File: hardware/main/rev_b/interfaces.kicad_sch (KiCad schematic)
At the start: 12 parts, among them U50 TCAN3413DR, U51 MCP2518FD-H/QBB, Y50 40MHz ABM8G

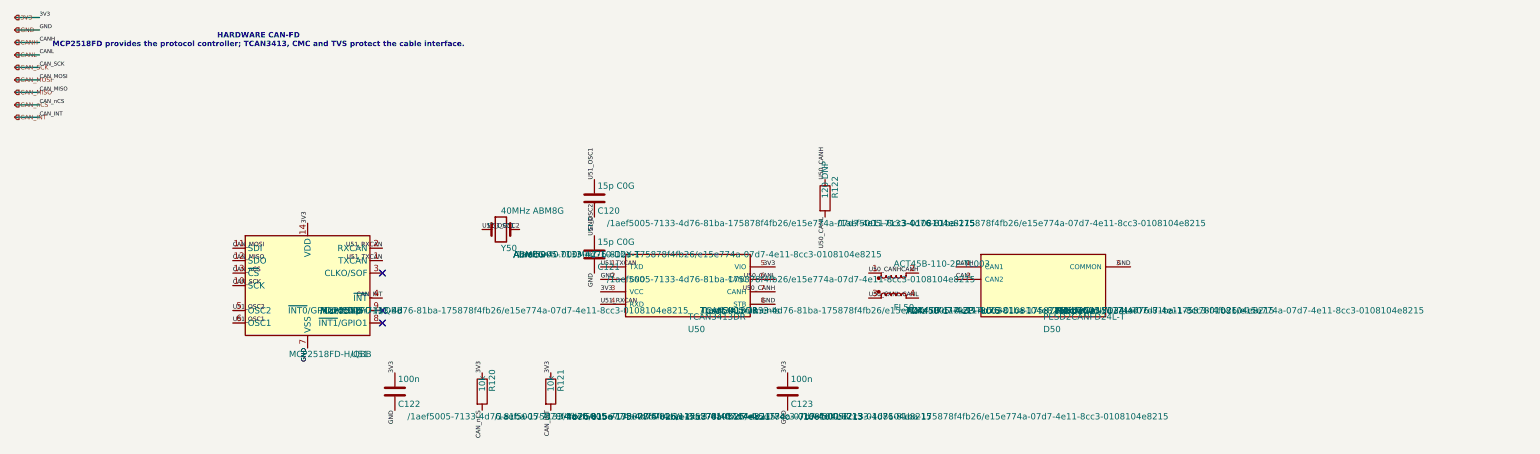
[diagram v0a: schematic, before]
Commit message: build: route and validate rev-b boards
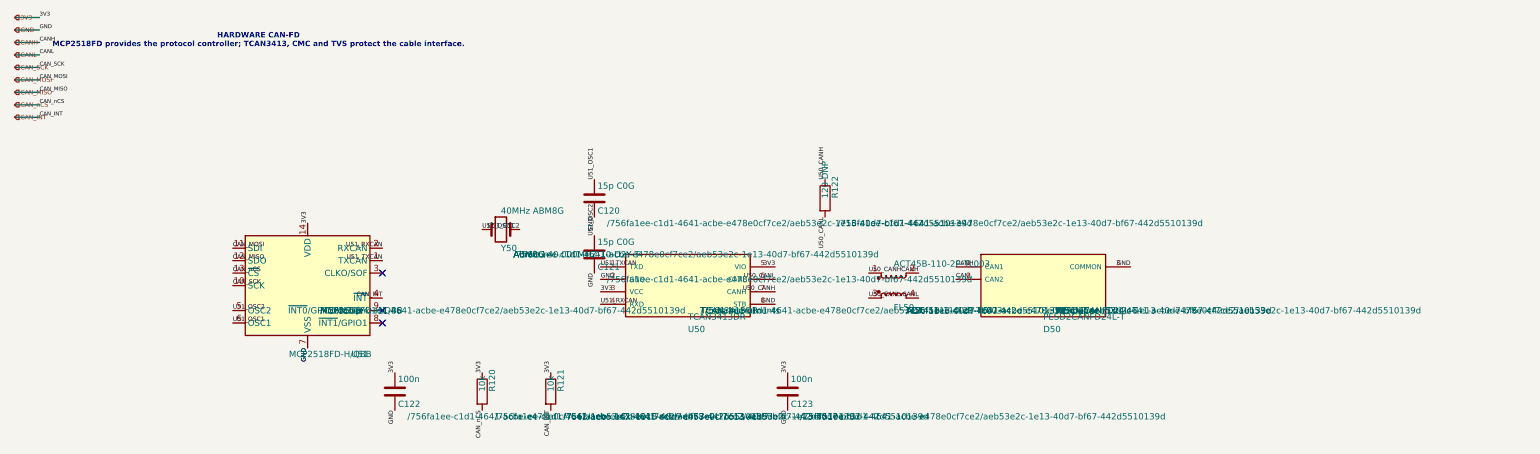
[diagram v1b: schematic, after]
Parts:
- C120, C121, C122, C123, D50, R120, R121, R122, U50, U51, Y50: hierarchy_path /1aef5005-7133-4d76-81ba-175878f4fb26/e15e774a-07d7-4e11-8c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 -> /756fa1ee-c1d1-4641-acbe-e478e0cf7ce2/aeb53e2c-1e13-40d7-bf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
- FL50: footprint Inductor_SMD:L_CommonModeChoke_Coilank_ACM4532 -> Inductor_SMD:L_CommonModeChoke_Coilcraft_1812CAN; hierarchy_path /1aef5005-7133-4d76-81ba-175878f4fb26/e15e774a-07d7-4e11-8c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 -> /756fa1ee-c1d1-4641-acbe-e478e0cf7ce2/aeb53e2c-1e13-40d7-bf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
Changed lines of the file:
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@@
 			)
 		)
-		(property "hierarchy_path" "/1aef5005-7133-4d76-81ba-175878f4fb26/e15e774a-07d7-4e11-8cc3-0108104e8215"
+		(property "hierarchy_path" "/756fa1ee-c1d1-4641-acbe-e478e0cf7ce2/aeb53e2c-1e13-40d7-bf67-442d5510139d"
 			(at 82.55 80.0099 0)
 			(effects
@@
 		(instances
 			(project "main_rev_b"
-				(path "/1aef5005-7133-4d76-81ba-175878f4fb26/e15e774a-07d7-4e11-8cc3-0108104e8215"
+				(path "/756fa1ee-c1d1-4641-acbe-e478e0cf7ce2/aeb53e2c-1e13-40d7-bf67-442d5510139d"
 					(reference "U51")
 					(unit 1)
@@
 			)
 		)
-		(property "hierarchy_path" "/1aef5005-7133-4d76-81ba-175878f4fb26/e15e774a-07d7-4e11-8cc3-0108104e8215"
+		(property "hierarchy_path" "/756fa1ee-c1d1-4641-acbe-e478e0cf7ce2/aeb53e2c-1e13-40d7-bf67-442d5510139d"
 			(at 121.92 68.5799 0)
 			(effects
@@
 		(instances
 			(project "main_rev_b"
-				(path "/1aef5005-7133-4d76-81ba-175878f4fb26/e15e774a-07d7-4e11-8cc3-0108104e8215"
+				(path "/756fa1ee-c1d1-4641-acbe-e478e0cf7ce2/aeb53e2c-1e13-40d7-bf67-442d5510139d"
 					(reference "Y50")
 					(unit 1)
@@
 			)
 		)
-		(property "hierarchy_path" "/1aef5005-7133-4d76-81ba-175878f4fb26/e15e774a-07d7-4e11-8cc3-0108104e8215"
+		(property "hierarchy_path" "/756fa1ee-c1d1-4641-acbe-e478e0cf7ce2/aeb53e2c-1e13-40d7-bf67-442d5510139d"
 			(at 140.97 62.2299 0)
 			(effects
@@
 		(instances
 			(project "main_rev_b"
-				(path "/1aef5005-7133-4d76-81ba-175878f4fb26/e15e774a-07d7-4e11-8cc3-0108104e8215"
+				(path "/756fa1ee-c1d1-4641-acbe-e478e0cf7ce2/aeb53e2c-1e13-40d7-bf67-442d5510139d"
 					(reference "C120")
 					(unit 1)
@@
 			)
 		)
-		(property "hierarchy_path" "/1aef5005-7133-4d76-81ba-175878f4fb26/e15e774a-07d7-4e11-8cc3-0108104e8215"
+		(property "hierarchy_path" "/756fa1ee-c1d1-4641-acbe-e478e0cf7ce2/aeb53e2c-1e13-40d7-bf67-442d5510139d"
 			(at 140.97 73.6599 0)
 			(effects
@@
 		(instances
 			(project "main_rev_b"
-				(path "/1aef5005-7133-4d76-81ba-175878f4fb26/e15e774a-07d7-4e11-8cc3-0108104e8215"
+				(path "/756fa1ee-c1d1-4641-acbe-e478e0cf7ce2/aeb53e2c-1e13-40d7-bf67-442d5510139d"
 					(reference "C121")
 					(unit 1)
@@
 			)
 		)
-		(property "hierarchy_path" "/1aef5005-7133-4d76-81ba-175878f4fb26/e15e774a-07d7-4e11-8cc3-0108104e8215"
+		(property "hierarchy_path" "/756fa1ee-c1d1-4641-acbe-e478e0cf7ce2/aeb53e2c-1e13-40d7-bf67-442d5510139d"
 			(at 100.33 101.5999 0)
 			(effects
@@
 		(instances
 			(project "main_rev_b"
-				(path "/1aef5005-7133-4d76-81ba-175878f4fb26/e15e774a-07d7-4e11-8cc3-0108104e8215"
+				(path "/756fa1ee-c1d1-4641-acbe-e478e0cf7ce2/aeb53e2c-1e13-40d7-bf67-442d5510139d"
 					(reference "C122")
 					(unit 1)
@@
 			)
 		)
-		(property "hierarchy_path" "/1aef5005-7133-4d76-81ba-175878f4fb26/e15e774a-07d7-4e11-8cc3-0108104e8215"
+		(property "hierarchy_path" "/756fa1ee-c1d1-4641-acbe-e478e0cf7ce2/aeb53e2c-1e13-40d7-bf67-442d5510139d"
 			(at 118.11 101.5999 0)
 			(effects
@@
 		(instances
 			(project "main_rev_b"
-				(path "/1aef5005-7133-4d76-81ba-175878f4fb26/e15e774a-07d7-4e11-8cc3-0108104e8215"
+				(path "/756fa1ee-c1d1-4641-acbe-e478e0cf7ce2/aeb53e2c-1e13-40d7-bf67-442d5510139d"
 					(reference "R120")
 					(unit 1)
@@
 			)
 		)
-		(property "hierarchy_path" "/1aef5005-7133-4d76-81ba-175878f4fb26/e15e774a-07d7-4e11-8cc3-0108104e8215"
+		(property "hierarchy_path" "/756fa1ee-c1d1-4641-acbe-e478e0cf7ce2/aeb53e2c-1e13-40d7-bf67-442d5510139d"
 			(at 132.08 101.5999 0)
 			(effects
@@
 		(instances
 			(project "main_rev_b"
-				(path "/1aef5005-7133-4d76-81ba-175878f4fb26/e15e774a-07d7-4e11-8cc3-0108104e8215"
+				(path "/756fa1ee-c1d1-4641-acbe-e478e0cf7ce2/aeb53e2c-1e13-40d7-bf67-442d5510139d"
 					(reference "R121")
 					(unit 1)
@@
 			)
 		)
-		(property "hierarchy_path" "/1aef5005-7133-4d76-81ba-175878f4fb26/e15e774a-07d7-4e11-8cc3-0108104e8215"
+		(property "hierarchy_path" "/756fa1ee-c1d1-4641-acbe-e478e0cf7ce2/aeb53e2c-1e13-40d7-bf67-442d5510139d"
 			(at 160.02 80.0099 0)
 			(effects
@@
 		(instances
 			(project "main_rev_b"
-				(path "/1aef5005-7133-4d76-81ba-175878f4fb26/e15e774a-07d7-4e11-8cc3-0108104e8215"
+				(path "/756fa1ee-c1d1-4641-acbe-e478e0cf7ce2/aeb53e2c-1e13-40d7-bf67-442d5510139d"
 					(reference "U50")
 					(unit 1)
@@
 			)
 		)
-		(property "hierarchy_path" "/1aef5005-7133-4d76-81ba-175878f4fb26/e15e774a-07d7-4e11-8cc3-0108104e8215"
+		(property "hierarchy_path" "/756fa1ee-c1d1-4641-acbe-e478e0cf7ce2/aeb53e2c-1e13-40d7-bf67-442d5510139d"
 			(at 180.34 101.5999 0)
 			(effects
@@
 		(instances
 			(project "main_rev_b"
-				(path "/1aef5005-7133-4d76-81ba-175878f4fb26/e15e774a-07d7-4e11-8cc3-0108104e8215"
+				(path "/756fa1ee-c1d1-4641-acbe-e478e0cf7ce2/aeb53e2c-1e13-40d7-bf67-442d5510139d"
 					(reference "C123")
 					(unit 1)
@@
 			)
 		)
-		(property "Footprint" "Inductor_SMD:L_CommonModeChoke_Coilank_ACM4532"
+		(property "Footprint" "Inductor_SMD:L_CommonModeChoke_Coilcraft_1812CAN"
 			(at 199.39 74.93 0.0000)
 			(effects
@@
 			)
 		)
-		(property "hierarchy_path" "/1aef5005-7133-4d76-81ba-175878f4fb26/e15e774a-07d7-4e11-8cc3-0108104e8215"
+		(property "hierarchy_path" "/756fa1ee-c1d1-4641-acbe-e478e0cf7ce2/aeb53e2c-1e13-40d7-bf67-442d5510139d"
 			(at 201.93 80.0099 0)
 			(effects
@@
 		(instances
 			(project "main_rev_b"
-				(path "/1aef5005-7133-4d76-81ba-175878f4fb26/e15e774a-07d7-4e11-8cc3-0108104e8215"
+				(path "/756fa1ee-c1d1-4641-acbe-e478e0cf7ce2/aeb53e2c-1e13-40d7-bf67-442d5510139d"
 					(reference "FL50")
 					(unit 1)
@@
 			)
 		)
-		(property "hierarchy_path" "/1aef5005-7133-4d76-81ba-175878f4fb26/e15e774a-07d7-4e11-8cc3-0108104e8215"
+		(property "hierarchy_path" "/756fa1ee-c1d1-4641-acbe-e478e0cf7ce2/aeb53e2c-1e13-40d7-bf67-442d5510139d"
 			(at 187.96 62.2299 0)
 			(effects
@@
 		(instances
 			(project "main_rev_b"
-				(path "/1aef5005-7133-4d76-81ba-175878f4fb26/e15e774a-07d7-4e11-8cc3-0108104e8215"
+				(path "/756fa1ee-c1d1-4641-acbe-e478e0cf7ce2/aeb53e2c-1e13-40d7-bf67-442d5510139d"
 					(reference "R122")
 					(unit 1)
@@
 			)
 		)
-		(property "hierarchy_path" "/1aef5005-7133-4d76-81ba-175878f4fb26/e15e774a-07d7-4e11-8cc3-0108104e8215"
+		(property "hierarchy_path" "/756fa1ee-c1d1-4641-acbe-e478e0cf7ce2/aeb53e2c-1e13-40d7-bf67-442d5510139d"
 			(at 232.41 80.0099 0)
 			(effects
@@
 		(instances
 			(project "main_rev_b"
-				(path "/1aef5005-7133-4d76-81ba-175878f4fb26/e15e774a-07d7-4e11-8cc3-0108104e8215"
+				(path "/756fa1ee-c1d1-4641-acbe-e478e0cf7ce2/aeb53e2c-1e13-40d7-bf67-442d5510139d"
 					(reference "D50")
 					(unit 1)

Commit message: build: route and validate rev-b boards
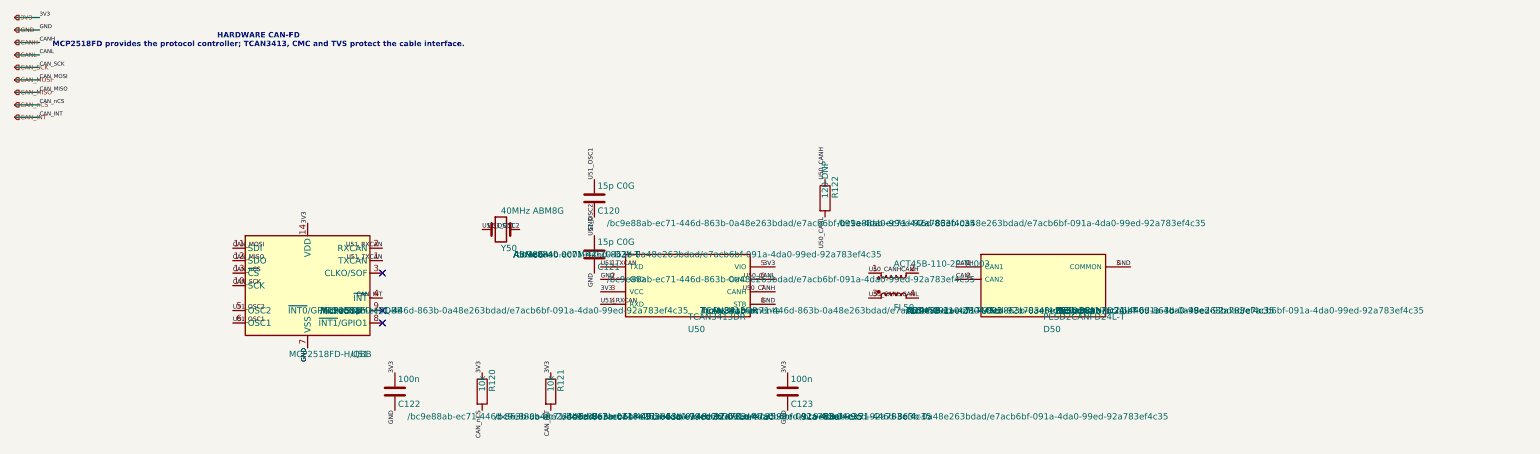
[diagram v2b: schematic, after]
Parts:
- C120, C121, C122, C123, D50, FL50, R120, R121, R122, U50, U51, Y50: hierarchy_path /756fa1ee-c1d1-4641-acbe-e478e0cf7ce2/aeb53e2c-1e13-40d7-bf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 -> /bc9e88ab-ec71-446d-863b-0a48e263bdad/e7acb6bf-091a-4da0-99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
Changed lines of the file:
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@@
 			)
 		)
-		(property "hierarchy_path" "/756fa1ee-c1d1-4641-acbe-e478e0cf7ce2/aeb53e2c-1e13-40d7-bf67-442d5510139d"
+		(property "hierarchy_path" "/bc9e88ab-ec71-446d-863b-0a48e263bdad/e7acb6bf-091a-4da0-99ed-92a783ef4c35"
 			(at 82.55 80.0099 0)
 			(effects
@@
 		(instances
 			(project "main_rev_b"
-				(path "/756fa1ee-c1d1-4641-acbe-e478e0cf7ce2/aeb53e2c-1e13-40d7-bf67-442d5510139d"
+				(path "/bc9e88ab-ec71-446d-863b-0a48e263bdad/e7acb6bf-091a-4da0-99ed-92a783ef4c35"
 					(reference "U51")
 					(unit 1)
@@
 			)
 		)
-		(property "hierarchy_path" "/756fa1ee-c1d1-4641-acbe-e478e0cf7ce2/aeb53e2c-1e13-40d7-bf67-442d5510139d"
+		(property "hierarchy_path" "/bc9e88ab-ec71-446d-863b-0a48e263bdad/e7acb6bf-091a-4da0-99ed-92a783ef4c35"
 			(at 121.92 68.5799 0)
 			(effects
@@
 		(instances
 			(project "main_rev_b"
-				(path "/756fa1ee-c1d1-4641-acbe-e478e0cf7ce2/aeb53e2c-1e13-40d7-bf67-442d5510139d"
+				(path "/bc9e88ab-ec71-446d-863b-0a48e263bdad/e7acb6bf-091a-4da0-99ed-92a783ef4c35"
 					(reference "Y50")
 					(unit 1)
@@
 			)
 		)
-		(property "hierarchy_path" "/756fa1ee-c1d1-4641-acbe-e478e0cf7ce2/aeb53e2c-1e13-40d7-bf67-442d5510139d"
+		(property "hierarchy_path" "/bc9e88ab-ec71-446d-863b-0a48e263bdad/e7acb6bf-091a-4da0-99ed-92a783ef4c35"
 			(at 140.97 62.2299 0)
 			(effects
@@
 		(instances
 			(project "main_rev_b"
-				(path "/756fa1ee-c1d1-4641-acbe-e478e0cf7ce2/aeb53e2c-1e13-40d7-bf67-442d5510139d"
+				(path "/bc9e88ab-ec71-446d-863b-0a48e263bdad/e7acb6bf-091a-4da0-99ed-92a783ef4c35"
 					(reference "C120")
 					(unit 1)
@@
 			)
 		)
-		(property "hierarchy_path" "/756fa1ee-c1d1-4641-acbe-e478e0cf7ce2/aeb53e2c-1e13-40d7-bf67-442d5510139d"
+		(property "hierarchy_path" "/bc9e88ab-ec71-446d-863b-0a48e263bdad/e7acb6bf-091a-4da0-99ed-92a783ef4c35"
 			(at 140.97 73.6599 0)
 			(effects
@@
 		(instances
 			(project "main_rev_b"
-				(path "/756fa1ee-c1d1-4641-acbe-e478e0cf7ce2/aeb53e2c-1e13-40d7-bf67-442d5510139d"
+				(path "/bc9e88ab-ec71-446d-863b-0a48e263bdad/e7acb6bf-091a-4da0-99ed-92a783ef4c35"
 					(reference "C121")
 					(unit 1)
@@
 			)
 		)
-		(property "hierarchy_path" "/756fa1ee-c1d1-4641-acbe-e478e0cf7ce2/aeb53e2c-1e13-40d7-bf67-442d5510139d"
+		(property "hierarchy_path" "/bc9e88ab-ec71-446d-863b-0a48e263bdad/e7acb6bf-091a-4da0-99ed-92a783ef4c35"
 			(at 100.33 101.5999 0)
 			(effects
@@
 		(instances
 			(project "main_rev_b"
-				(path "/756fa1ee-c1d1-4641-acbe-e478e0cf7ce2/aeb53e2c-1e13-40d7-bf67-442d5510139d"
+				(path "/bc9e88ab-ec71-446d-863b-0a48e263bdad/e7acb6bf-091a-4da0-99ed-92a783ef4c35"
 					(reference "C122")
 					(unit 1)
@@
 			)
 		)
-		(property "hierarchy_path" "/756fa1ee-c1d1-4641-acbe-e478e0cf7ce2/aeb53e2c-1e13-40d7-bf67-442d5510139d"
+		(property "hierarchy_path" "/bc9e88ab-ec71-446d-863b-0a48e263bdad/e7acb6bf-091a-4da0-99ed-92a783ef4c35"
 			(at 118.11 101.5999 0)
 			(effects
@@
 		(instances
 			(project "main_rev_b"
-				(path "/756fa1ee-c1d1-4641-acbe-e478e0cf7ce2/aeb53e2c-1e13-40d7-bf67-442d5510139d"
+				(path "/bc9e88ab-ec71-446d-863b-0a48e263bdad/e7acb6bf-091a-4da0-99ed-92a783ef4c35"
 					(reference "R120")
 					(unit 1)
@@
 			)
 		)
-		(property "hierarchy_path" "/756fa1ee-c1d1-4641-acbe-e478e0cf7ce2/aeb53e2c-1e13-40d7-bf67-442d5510139d"
+		(property "hierarchy_path" "/bc9e88ab-ec71-446d-863b-0a48e263bdad/e7acb6bf-091a-4da0-99ed-92a783ef4c35"
 			(at 132.08 101.5999 0)
 			(effects
@@
 		(instances
 			(project "main_rev_b"
-				(path "/756fa1ee-c1d1-4641-acbe-e478e0cf7ce2/aeb53e2c-1e13-40d7-bf67-442d5510139d"
+				(path "/bc9e88ab-ec71-446d-863b-0a48e263bdad/e7acb6bf-091a-4da0-99ed-92a783ef4c35"
 					(reference "R121")
 					(unit 1)
@@
 			)
 		)
-		(property "hierarchy_path" "/756fa1ee-c1d1-4641-acbe-e478e0cf7ce2/aeb53e2c-1e13-40d7-bf67-442d5510139d"
+		(property "hierarchy_path" "/bc9e88ab-ec71-446d-863b-0a48e263bdad/e7acb6bf-091a-4da0-99ed-92a783ef4c35"
 			(at 160.02 80.0099 0)
 			(effects
@@
 		(instances
 			(project "main_rev_b"
-				(path "/756fa1ee-c1d1-4641-acbe-e478e0cf7ce2/aeb53e2c-1e13-40d7-bf67-442d5510139d"
+				(path "/bc9e88ab-ec71-446d-863b-0a48e263bdad/e7acb6bf-091a-4da0-99ed-92a783ef4c35"
 					(reference "U50")
 					(unit 1)
@@
 			)
 		)
-		(property "hierarchy_path" "/756fa1ee-c1d1-4641-acbe-e478e0cf7ce2/aeb53e2c-1e13-40d7-bf67-442d5510139d"
+		(property "hierarchy_path" "/bc9e88ab-ec71-446d-863b-0a48e263bdad/e7acb6bf-091a-4da0-99ed-92a783ef4c35"
 			(at 180.34 101.5999 0)
 			(effects
@@
 		(instances
 			(project "main_rev_b"
-				(path "/756fa1ee-c1d1-4641-acbe-e478e0cf7ce2/aeb53e2c-1e13-40d7-bf67-442d5510139d"
+				(path "/bc9e88ab-ec71-446d-863b-0a48e263bdad/e7acb6bf-091a-4da0-99ed-92a783ef4c35"
 					(reference "C123")
 					(unit 1)
@@
 			)
 		)
-		(property "hierarchy_path" "/756fa1ee-c1d1-4641-acbe-e478e0cf7ce2/aeb53e2c-1e13-40d7-bf67-442d5510139d"
+		(property "hierarchy_path" "/bc9e88ab-ec71-446d-863b-0a48e263bdad/e7acb6bf-091a-4da0-99ed-92a783ef4c35"
 			(at 201.93 80.0099 0)
 			(effects
@@
 		(instances
 			(project "main_rev_b"
-				(path "/756fa1ee-c1d1-4641-acbe-e478e0cf7ce2/aeb53e2c-1e13-40d7-bf67-442d5510139d"
+				(path "/bc9e88ab-ec71-446d-863b-0a48e263bdad/e7acb6bf-091a-4da0-99ed-92a783ef4c35"
 					(reference "FL50")
 					(unit 1)
@@
 			)
 		)
-		(property "hierarchy_path" "/756fa1ee-c1d1-4641-acbe-e478e0cf7ce2/aeb53e2c-1e13-40d7-bf67-442d5510139d"
+		(property "hierarchy_path" "/bc9e88ab-ec71-446d-863b-0a48e263bdad/e7acb6bf-091a-4da0-99ed-92a783ef4c35"
 			(at 187.96 62.2299 0)
 			(effects
@@
 		(instances
 			(project "main_rev_b"
-				(path "/756fa1ee-c1d1-4641-acbe-e478e0cf7ce2/aeb53e2c-1e13-40d7-bf67-442d5510139d"
+				(path "/bc9e88ab-ec71-446d-863b-0a48e263bdad/e7acb6bf-091a-4da0-99ed-92a783ef4c35"
 					(reference "R122")
 					(unit 1)
@@
 			)
 		)
-		(property "hierarchy_path" "/756fa1ee-c1d1-4641-acbe-e478e0cf7ce2/aeb53e2c-1e13-40d7-bf67-442d5510139d"
+		(property "hierarchy_path" "/bc9e88ab-ec71-446d-863b-0a48e263bdad/e7acb6bf-091a-4da0-99ed-92a783ef4c35"
 			(at 232.41 80.0099 0)
 			(effects
@@
 		(instances
 			(project "main_rev_b"
-				(path "/756fa1ee-c1d1-4641-acbe-e478e0cf7ce2/aeb53e2c-1e13-40d7-bf67-442d5510139d"
+				(path "/bc9e88ab-ec71-446d-863b-0a48e263bdad/e7acb6bf-091a-4da0-99ed-92a783ef4c35"
 					(reference "D50")
 					(unit 1)
